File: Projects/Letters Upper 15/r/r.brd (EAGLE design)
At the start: 16.2 x 21.6 mm, 42 parts

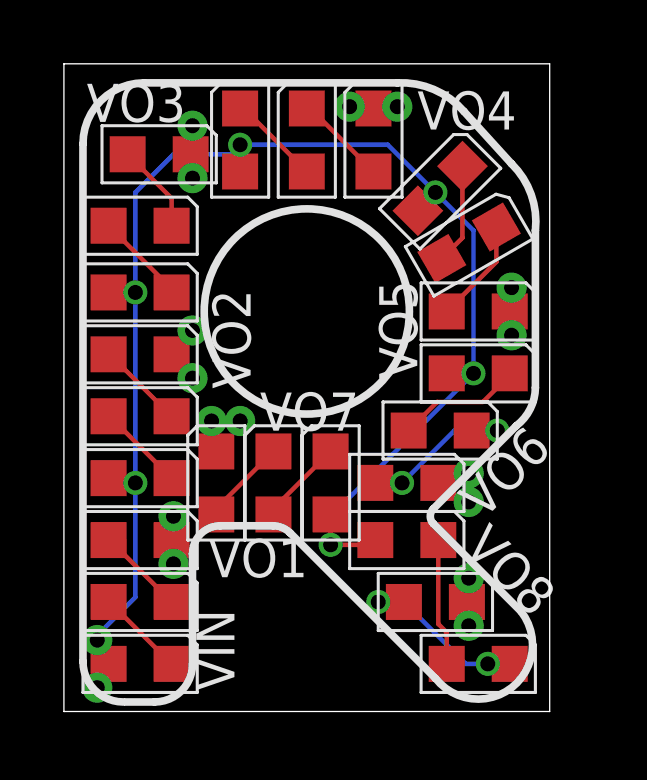
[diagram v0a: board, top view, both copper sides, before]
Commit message: 
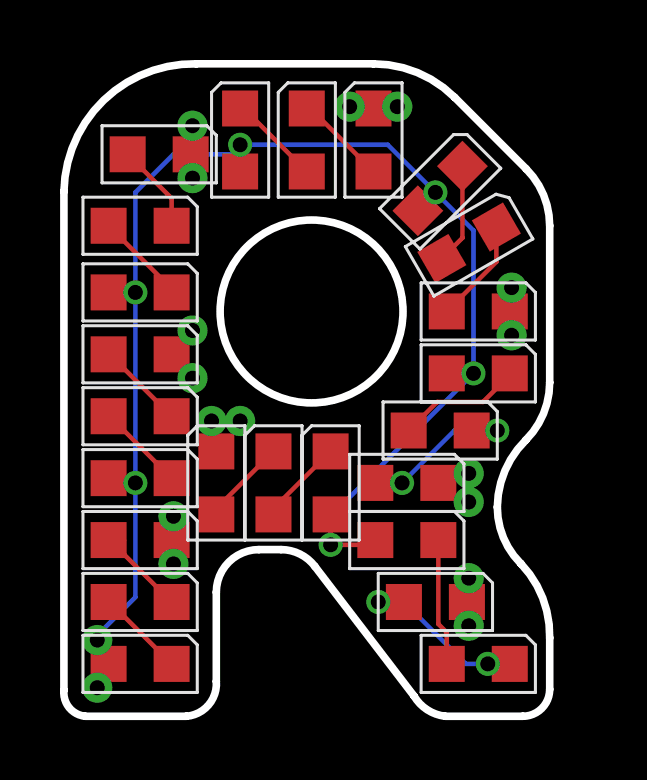
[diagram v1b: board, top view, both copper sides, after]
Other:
- board size 16.2 x 21.6 mm -> 16.2 x 21.7 mm
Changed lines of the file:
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@@
 <layer number="18" name="Vias" color="2" fill="1" visible="yes" active="yes"/>
 <layer number="19" name="Unrouted" color="6" fill="1" visible="yes" active="yes"/>
-<layer number="20" name="Dimension" color="15" fill="1" visible="yes" active="yes"/>
+<layer number="20" name="Dimension" color="3" fill="1" visible="yes" active="yes"/>
 <layer number="21" name="tPlace" color="7" fill="1" visible="yes" active="yes"/>
 <layer number="22" name="bPlace" color="7" fill="1" visible="yes" active="yes"/>
@@
 <layer number="24" name="bOrigins" color="15" fill="1" visible="yes" active="yes"/>
 <layer number="25" name="tNames" color="7" fill="1" visible="yes" active="yes"/>
-<layer number="26" name="bNames" color="7" fill="1" visible="yes" active="yes"/>
+<layer number="26" name="bNames" color="5" fill="1" visible="yes" active="yes"/>
 <layer number="27" name="tValues" color="7" fill="1" visible="yes" active="yes"/>
 <layer number="28" name="bValues" color="7" fill="1" visible="yes" active="yes"/>
@@
 <board>
 <plain>
-<wire x1="0" y1="0" x2="16.1925" y2="0" width="0" layer="20"/>
-<wire x1="16.1925" y1="0" x2="16.1925" y2="21.59" width="0" layer="20"/>
-<wire x1="16.1925" y1="21.59" x2="0" y2="21.59" width="0" layer="20"/>
-<wire x1="0" y1="21.59" x2="0" y2="0" width="0" layer="20"/>
 <text x="0.9525" y="0.3175" size="20.32" layer="201" font="fixed" ratio="15" distance="27">R</text>
-<wire x1="0.635" y1="18.922009375" x2="0.635" y2="1.6645375" width="0.254" layer="21"/>
-<wire x1="0.635" y1="1.6645375" x2="1.9820375" y2="0.3175" width="0.254" layer="21" curve="90"/>
-<wire x1="0.635" y1="18.922009375" x2="2.667990625" y2="20.955" width="0.254" layer="21" curve="-90"/>
-<wire x1="2.667990625" y1="20.955" x2="11.1125" y2="20.955" width="0.254" layer="21"/>
-<wire x1="3.025096875" y1="0.3175" x2="4.28625" y2="1.578653125" width="0.254" layer="21" curve="90"/>
-<wire x1="12.31600625" y1="6.75975625" x2="15.08125" y2="9.525" width="0.254" layer="21"/>
-<wire x1="12.3825" y1="1.11125" x2="15.24" y2="3.33375" width="0.254" layer="21" curve="180"/>
-<wire x1="11.1125" y1="20.955" x2="13.335" y2="20.0025" width="0.254" layer="21" curve="-51.842773"/>
-<wire x1="14.9225" y1="18.25625" x2="15.71625" y2="16.03375" width="0.254" layer="21" curve="-51.842773"/>
-<wire x1="15.71625" y1="10.795" x2="15.08125" y2="9.525" width="0.254" layer="21" curve="-51.842773"/>
-<wire x1="15.71625" y1="10.795" x2="15.71625" y2="16.03375" width="0.254" layer="21"/>
-<wire x1="14.9225" y1="18.25625" x2="13.335" y2="20.0025" width="0.254" layer="21"/>
-<circle x="8.09625" y="13.335" radius="3.419578125" width="0.254" layer="21"/>
-<wire x1="13.0175" y1="7.46125" x2="12.065" y2="6.50875" width="0.254" layer="22"/>
-<wire x1="12.31600625" y1="6.75975625" x2="12.31600625" y2="6.25774375" width="0.254" layer="21" curve="90"/>
-<wire x1="12.31600625" y1="6.25774375" x2="15.24" y2="3.33375" width="0.254" layer="21"/>
-<wire x1="12.3825" y1="1.11125" x2="7.5395875" y2="5.9541625" width="0.254" layer="21"/>
-<wire x1="7.5395875" y1="5.9541625" x2="6.96720625" y2="6.19125" width="0.254" layer="21" curve="45"/>
-<wire x1="6.96720625" y1="6.19125" x2="5.2119125" y2="6.19125" width="0.254" layer="21"/>
-<wire x1="5.2119125" y1="6.19125" x2="4.28625" y2="5.2655875" width="0.254" layer="21" curve="90"/>
-<wire x1="4.28625" y1="5.2655875" x2="4.28625" y2="1.5875" width="0.254" layer="21"/>
-<wire x1="3.01625" y1="0.3175" x2="2.06375" y2="0.3175" width="0.254" layer="21"/>
+<wire x1="0" y1="17.334509375" x2="0" y2="0.70995" width="0.254" layer="20"/>
+<wire x1="0" y1="0.70995" x2="0.70995" y2="-0.15875" width="0.254" layer="20" curve="90"/>
+<wire x1="0.70995" y1="-0.15875" x2="4.075978125" y2="-0.15875" width="0.254" layer="20"/>
+<wire x1="4.075978125" y1="-0.15875" x2="5.08" y2="1.004021875" width="0.254" layer="20" curve="90"/>
+<wire x1="5.08" y1="1.004021875" x2="5.08" y2="3.977596875" width="0.254" layer="20"/>
+<wire x1="0" y1="17.334509375" x2="4.414240625" y2="21.59" width="0.254" layer="20" curve="-90"/>
+<wire x1="13.03085625" y1="20.46539375" x2="15.406728125" y2="18.089521875" width="0.254" layer="20"/>
+<wire x1="15.406728125" y1="18.089521875" x2="16.1925" y2="16.1925" width="0.254" layer="20" curve="-45"/>
+<wire x1="13.03085625" y1="20.46539375" x2="10.315815625" y2="21.59" width="0.254" layer="20" curve="44.999953"/>
+<wire x1="10.315815625" y1="21.59" x2="4.414240625" y2="21.59" width="0.254" layer="20"/>
+<wire x1="15.235071875" y1="4.926178125" x2="15.223259375" y2="4.937990625" width="0.254" layer="20"/>
+<wire x1="15.223259375" y1="4.937990625" x2="14.44625" y2="6.81385625" width="0.254" layer="20" curve="-45"/>
+<wire x1="14.44625" y1="6.81385625" x2="15.3995375" y2="9.0495375" width="0.254" layer="20" curve="-45"/>
+<wire x1="15.3995375" y1="9.0495375" x2="15.3979625" y2="9.0479625" width="0.254" layer="20"/>
+<wire x1="15.3979625" y1="9.0479625" x2="15.3995375" y2="9.0495375" width="0.254" layer="20" curve="0.047045"/>
+<wire x1="15.3995375" y1="9.0495375" x2="16.1925" y2="10.96614375" width="0.254" layer="20" curve="44.952955"/>
+<wire x1="16.1925" y1="10.96614375" x2="16.1925" y2="16.1925" width="0.254" layer="20"/>
+<circle x="8.255" y="13.335" radius="3.048" width="0.254" layer="20"/>
+<wire x1="5.08" y1="3.977596875" x2="6.499903125" y2="5.3975" width="0.254" layer="20" curve="-90"/>
+<wire x1="6.499903125" y1="5.3975" x2="7.235821875" y2="5.3975" width="0.254" layer="20"/>
+<wire x1="7.235821875" y1="5.3975" x2="8.363734375" y2="4.840115625" width="0.254" layer="20" curve="-52.594726"/>
+<wire x1="8.363734375" y1="4.840115625" x2="11.67203125" y2="0.51388125" width="0.254" layer="20"/>
+<wire x1="11.67203125" y1="0.51388125" x2="12.7119125" y2="-0.15875" width="0.254" layer="20" curve="52.59465"/>
+<wire x1="12.7119125" y1="-0.15875" x2="15.294475" y2="-0.15875" width="0.254" layer="20"/>
+<wire x1="15.294475" y1="-0.15875" x2="16.1925" y2="0.739275" width="0.254" layer="20" curve="90"/>
+<wire x1="16.1925" y1="0.739275" x2="16.1925" y2="2.45599375" width="0.254" layer="20"/>
+<wire x1="16.1925" y1="2.45599375" x2="15.235071875" y2="4.926178125" width="0.254" layer="20" curve="45"/>
 </plain>
 <attributes>
@@
 </element>
 <element name="VIN" library="CyberRailGuru" package="P1-20" value="" x="1.11125" y="0.79375" smashed="yes">
-<attribute name="NAME" x="5.68325" y="0.6985" size="1.27" layer="25" ratio="15" rot="R90"/>
+<attribute name="NAME" x="3.175" y="0.3175" size="1.27" layer="26" ratio="15" rot="R90"/>
 <attribute name="VALUE" x="-0.41275" y="-1.23825" size="1.27" layer="27" ratio="10"/>
 </element>
 <element name="VO1" library="CyberRailGuru" package="P1-20" value="" x="3.65125" y="4.92125" smashed="yes">
-<attribute name="NAME" x="4.826" y="4.47675" size="1.27" layer="25" ratio="15"/>
+<attribute name="NAME" x="2.8575" y="4.1275" size="1.27" layer="26" ratio="15" rot="R90"/>
 <attribute name="VALUE" x="2.12725" y="2.88925" size="1.27" layer="27" ratio="10"/>
 </element>
 <element name="VO2" library="CyberRailGuru" package="P1-20" value="" x="4.28625" y="12.7" smashed="yes">
-<attribute name="NAME" x="4.953" y="14.06525" size="1.27" layer="25" ratio="15" rot="R270"/>
+<attribute name="NAME" x="3.4925" y="10.16" size="1.27" layer="26" ratio="15" rot="R90"/>
 <attribute name="VALUE" x="2.76225" y="10.668" size="1.27" layer="27" ratio="10"/>
 </element>
 <element name="VO3" library="CyberRailGuru" package="P1-20" value="" x="4.28625" y="19.52625" smashed="yes">
-<attribute name="NAME" x="4.064" y="20.92325" size="1.27" layer="25" ratio="15" rot="R180"/>
+<attribute name="NAME" x="6.35" y="17.145" size="1.27" layer="26" ratio="15" rot="R90"/>
 <attribute name="VALUE" x="2.76225" y="17.49425" size="1.27" layer="27" ratio="10"/>
 </element>
 <element name="VO4" library="CyberRailGuru" package="P1-20" value="" x="9.525" y="20.16125" smashed="yes">
-<attribute name="NAME" x="11.7837625" y="19.39925" size="1.27" layer="25" ratio="15"/>
+<attribute name="NAME" x="8.5725" y="18.0975" size="1.27" layer="26" ratio="15"/>
 <attribute name="VALUE" x="8.001" y="18.12925" size="1.27" layer="27" ratio="10"/>
 </element>
 <element name="VO5" library="CyberRailGuru" package="P1-20" value="" x="14.9225" y="12.54125" smashed="yes">
-<attribute name="NAME" x="10.50925" y="14.38275" size="1.27" layer="25" ratio="15" rot="R270"/>
+<attribute name="NAME" x="14.2875" y="11.7475" size="1.27" layer="26" ratio="15" rot="R90"/>
 <attribute name="VALUE" x="13.3985" y="10.50925" size="1.27" layer="27" ratio="10"/>
 </element>
 <element name="VO6" library="CyberRailGuru" package="P1-20" value="" x="13.49375" y="7.9375" smashed="yes">
-<attribute name="NAME" x="13.973190625" y="6.370853125" size="1.27" layer="25" ratio="15" rot="R45"/>
+<attribute name="NAME" x="12.7" y="6.0325" size="1.27" layer="26" ratio="15" rot="R90"/>
 <attribute name="VALUE" x="11.96975" y="5.9055" size="1.27" layer="27" ratio="10"/>
 </element>
 <element name="VO7" library="CyberRailGuru" package="P1-20" value="" x="4.92125" y="9.68375" smashed="yes">
-<attribute name="NAME" x="6.534390625" y="9.3614625" size="1.27" layer="25" ratio="15"/>
+<attribute name="NAME" x="4.1275" y="7.62" size="1.27" layer="26" ratio="15"/>
 <attribute name="VALUE" x="3.39725" y="7.65175" size="1.27" layer="27" ratio="10"/>
 </element>
@@
 </element>
 <element name="VO8" library="CyberRailGuru" package="P1-20" value="" x="13.49375" y="4.445" smashed="yes">
-<attribute name="NAME" x="16.508403125" y="3.9912" size="1.27" layer="25" ratio="15" rot="R135"/>
+<attribute name="NAME" x="12.7" y="1.905" size="1.27" layer="26" ratio="15" rot="R90"/>
 <attribute name="VALUE" x="11.96975" y="2.413" size="1.27" layer="27" ratio="10"/>
 </element>
